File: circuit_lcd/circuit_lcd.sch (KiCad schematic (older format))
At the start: 24 parts, among them J1 Conn_01x04, J2 Conn_01x01, J3 Conn_01x04, J4 Conn_01x04, J5 Conn_01x01, J6 Conn_01x01, J7 Conn_01x01, M1 Stepper_Motor_bipolar, U3 HT1621B, U5 VIM-878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

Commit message: Removed contrast pot and renamed segment nets
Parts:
- removed RV2: R_POT, Potentiometer_THT:Potentiometer_Bourns_3266Y_Vertical, symbol Device:R_POT
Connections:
- wire segments 44 -> 41
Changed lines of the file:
@@
 EESchema Schematic File Version 4
-LIBS:circuit_lcd-cache
 EELAYER 26 0
 EELAYER END
@@
 L power:+5V #PWR0103
 U 1 1 5CD2DDE9
-P 1400 5300
-F 0 "#PWR0103" H 1400 5150 50  0001 C CNN
-F 1 "+5V" H 1415 5473 50  0000 C CNN
-F 2 "" H 1400 5300 50  0001 C CNN
-F 3 "" H 1400 5300 50  0001 C CNN
-	1    1400 5300
-	1    0    0    -1
-$EndComp
-$Comp
-L Device:R_POT RV2
-U 1 1 5CD2FBF5
-P 1400 5550
-F 0 "RV2" H 1330 5596 50  0000 R CNN
-F 1 "R_POT" H 1330 5505 50  0000 R CNN
-F 2 "Potentiometer_THT:Potentiometer_Bourns_3266Y_Vertical" H 1400 5550 50  0001 C CNN
-F 3 "~" H 1400 5550 50  0001 C CNN
-	1    1400 5550
-	1    0    0    -1
-$EndComp
-Wire Wire Line
-	1400 5300 1400 5350
-Wire Wire Line
-	1750 5350 1750 5650
-Wire Wire Line
-	1750 5650 2050 5650
-Connection ~ 1400 5350
-Wire Wire Line
-	1400 5350 1400 5400
-$Comp
-L power:GND #PWR0104
-U 1 1 5CD324BD
-P 1400 5700
-F 0 "#PWR0104" H 1400 5450 50  0001 C CNN
-F 1 "GND" H 1405 5527 50  0000 C CNN
-F 2 "" H 1400 5700 50  0001 C CNN
-F 3 "" H 1400 5700 50  0001 C CNN
-	1    1400 5700
-	1    0    0    -1
-$EndComp
-Wire Wire Line
-	1400 5350 1750 5350
-Wire Wire Line
-	1550 5550 2050 5550
+P 1550 5550
+F 0 "#PWR0103" H 1550 5400 50  0001 C CNN
+F 1 "+5V" H 1565 5723 50  0000 C CNN
+F 2 "" H 1550 5550 50  0001 C CNN
+F 3 "" H 1550 5550 50  0001 C CNN
+	1    1550 5550
+	1    0    0    -1
+$EndComp
 $Comp
 L Motor:Stepper_Motor_bipolar M1
@@
 	8050 3750 8050 3850
 Connection ~ 8050 3850
+Text Label 2050 4750 2    50   ~ 0
+SEG0
+Text Label 2050 4650 2    50   ~ 0
+SEG1
+Text Label 2050 4550 2    50   ~ 0
+SEG2
+Text Label 2050 4450 2    50   ~ 0
+SEG3
+Text Label 2050 4350 2    50   ~ 0
+SEG4
+Text Label 2050 4250 2    50   ~ 0
+SEG5
+Text Label 2050 4150 2    50   ~ 0
+SEG6
+Text Label 2050 4050 2    50   ~ 0
+SEG7
 Text Label 3250 4050 0    50   ~ 0
-SEG0
+SEG8
 Text Label 3250 4150 0    50   ~ 0
-SEG1
+SEG9
 Text Label 3250 4250 0    50   ~ 0
-SEG2
+SEG10
 Text Label 3250 4350 0    50   ~ 0
-SEG3
+SEG11
 Text Label 3250 4450 0    50   ~ 0
-SEG4
+SEG12
 Text Label 3250 4550 0    50   ~ 0
-SEG5
+SEG13
 Text Label 3250 4650 0    50   ~ 0
-SEG6
+SEG14
 Text Label 3250 4750 0    50   ~ 0
-SEG7
-Text Label 2050 4050 2    50   ~ 0
-SEG8
-Text Label 2050 4150 2    50   ~ 0
-SEG9
-Text Label 2050 4250 2    50   ~ 0
-SEG10
-Text Label 2050 4350 2    50   ~ 0
-SEG11
-Text Label 2050 4450 2    50   ~ 0
-SEG12
-Text Label 2050 4550 2    50   ~ 0
-SEG13
-Text Label 2050 4650 2    50   ~ 0
-SEG14
-Text Label 2050 4750 2    50   ~ 0
 SEG15
 Text Label 3250 4850 0    50   ~ 0
@@
 Text Label 5900 5800 0    50   ~ 0
 COM3
+Text Label 4750 5900 2    50   ~ 0
+SEG0
+Text Label 4750 5800 2    50   ~ 0
+SEG1
+Text Label 4750 5700 2    50   ~ 0
+SEG2
+Text Label 4750 5600 2    50   ~ 0
+SEG3
+Text Label 4750 5500 2    50   ~ 0
+SEG4
+Text Label 4750 5400 2    50   ~ 0
+SEG5
+Text Label 4750 5300 2    50   ~ 0
+SEG6
+Text Label 4750 5200 2    50   ~ 0
+SEG7
 Text Label 4750 4400 2    50   ~ 0
-SEG0
+SEG8
 Text Label 4750 4500 2    50   ~ 0
-SEG1
+SEG9
 Text Label 4750 4600 2    50   ~ 0
-SEG2
+SEG10
 Text Label 4750 4700 2    50   ~ 0
-SEG3
+SEG11
 Text Label 4750 4800 2    50   ~ 0
-SEG4
+SEG12
 Text Label 4750 4900 2    50   ~ 0
-SEG5
+SEG13
 Text Label 4750 5000 2    50   ~ 0
-SEG6
+SEG14
 Text Label 4750 5100 2    50   ~ 0
-SEG7
-Text Label 4750 5200 2    50   ~ 0
-SEG8
-Text Label 4750 5300 2    50   ~ 0
-SEG9
-Text Label 4750 5400 2    50   ~ 0
-SEG10
-Text Label 4750 5500 2    50   ~ 0
-SEG11
-Text Label 4750 5600 2    50   ~ 0
-SEG12
-Text Label 4750 5700 2    50   ~ 0
-SEG13
-Text Label 4750 5800 2    50   ~ 0
-SEG14
-Text Label 4750 5900 2    50   ~ 0
 SEG15
 Text Label 5900 4400 0    50   ~ 0
@@
 	-1   0    0    1
 $EndComp
+Wire Wire Line
+	2050 5550 1550 5550
+Wire Wire Line
+	1550 5650 1550 5550
+Wire Wire Line
+	1550 5650 2050 5650
+Connection ~ 1550 5550
 $EndSCHEMATC

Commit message: Added missing segments
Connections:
- net COM1: now also U5.18 (COM1); no longer U5.20 (COM3)
- net COM2: now also U5.19 (COM2); no longer U5.21 (DP8)
- net COM3: now also U5.20 (COM3); no longer U5.22 (8M)
- net SEG31: now reaches U3.25 (SEG31)
- net SEG31: now also U5.21 (DP8)
- net SEG30: now reaches U3.26 (SEG30)
- net SEG30: now also U5.22 (8M)
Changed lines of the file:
@@
 Text Label 4750 6000 2    50   ~ 0
 COM0
+Text Label 4750 6100 2    50   ~ 0
+COM1
+Text Label 5900 6100 0    50   ~ 0
+COM2
 Text Label 5900 6000 0    50   ~ 0
-COM1
-Text Label 5900 5900 0    50   ~ 0
-COM2
-Text Label 5900 5800 0    50   ~ 0
 COM3
 Text Label 4750 5900 2    50   ~ 0
@@
 	1550 5650 2050 5650
 Connection ~ 1550 5550
+Text Label 3250 6250 0    50   ~ 0
+SEG30
+Text Label 3250 6350 0    50   ~ 0
+SEG31
+Text Label 5900 5900 0    50   ~ 0
+SEG31
+Text Label 5900 5800 0    50   ~ 0
+SEG30
 $EndSCHEMATC

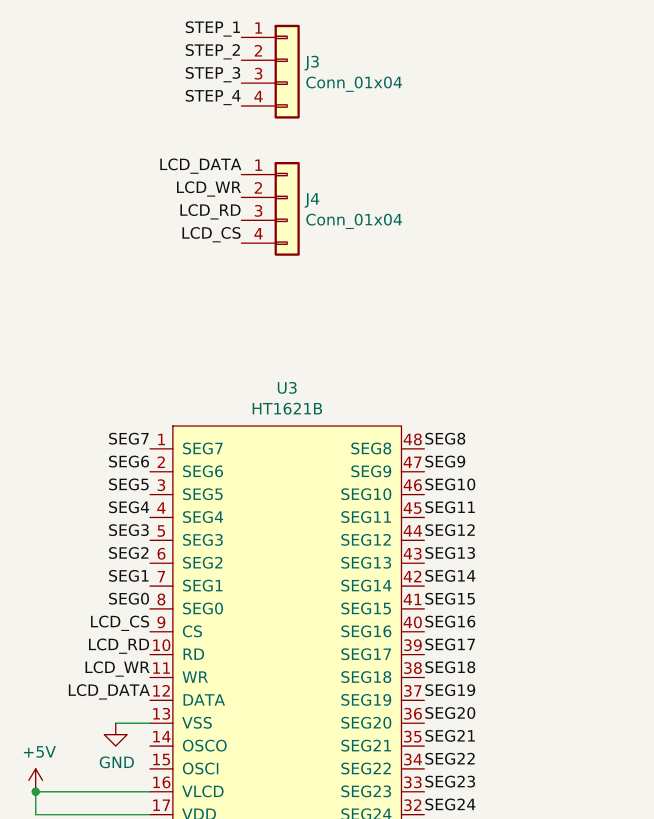
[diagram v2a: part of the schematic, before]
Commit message: Removed unused LCD read net
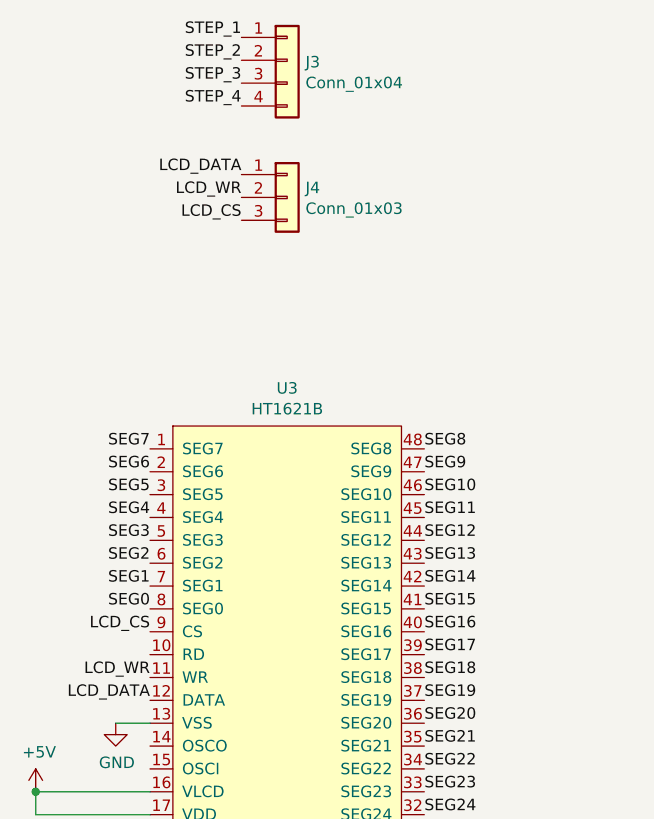
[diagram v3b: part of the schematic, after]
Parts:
- removed J4: Conn_01x04, Connector_PinSocket_2.54mm:PinSocket_1x04_P2.54mm_Vertical, symbol Connector_Generic:Conn_01x04
- added J4: Conn_01x03, Connector_PinSocket_2.54mm:PinSocket_1x03_P2.54mm_Vertical, symbol Connector_Generic:Conn_01x03
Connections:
- net LCD_CS: now also J4.3 (Pin_3)
- net LCD_DATA: now also J4.1 (Pin_1)
- net LCD_WR: now also J4.2 (Pin_2)
- net LCD_RD: no longer names the net of U3.10 (RD)
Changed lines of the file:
@@
 Text Label 2050 4850 2    50   ~ 0
 LCD_CS
-Text Label 2050 4950 2    50   ~ 0
-LCD_RD
 Text Label 2050 5050 2    50   ~ 0
 LCD_WR
@@
 Text Notes 7250 3450 0    50   ~ 0
 TODO: can the stepper be directly driven, maybe just add diodes
-Text Label 2450 3150 2    50   ~ 0
+Text Label 2450 3050 2    50   ~ 0
 LCD_CS
-Text Label 2450 3050 2    50   ~ 0
-LCD_RD
 Text Label 2450 2950 2    50   ~ 0
 LCD_WR
@@
 Text Notes 6050 2650 0    50   ~ 0
 Turn Signals
-$Comp
-L Connector_Generic:Conn_01x04 J4
-U 1 1 5D1C6209
-P 2650 2950
-F 0 "J4" H 2730 2942 50  0000 L CNN
-F 1 "Conn_01x04" H 2730 2851 50  0000 L CNN
-F 2 "Connector_PinSocket_2.54mm:PinSocket_1x04_P2.54mm_Vertical" H 2650 2950 50  0001 C CNN
-F 3 "~" H 2650 2950 50  0001 C CNN
-	1    2650 2950
-	1    0    0    -1
-$EndComp
 $Comp
 L Connector_Generic:Conn_01x04 J3
@@
 Text Label 5900 5800 0    50   ~ 0
 SEG30
+$Comp
+L Connector_Generic:Conn_01x03 J4
+U 1 1 5D29DC01
+P 2650 2950
+F 0 "J4" H 2730 2992 50  0000 L CNN
+F 1 "Conn_01x03" H 2730 2901 50  0000 L CNN
+F 2 "Connector_PinSocket_2.54mm:PinSocket_1x03_P2.54mm_Vertical" H 2650 2950 50  0001 C CNN
+F 3 "~" H 2650 2950 50  0001 C CNN
+	1    2650 2950
+	1    0    0    -1
+$EndComp
 $EndSCHEMATC
